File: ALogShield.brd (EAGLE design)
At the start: 53.3 x 78.5 mm, 32 parts, among them U1 DS3231MZ/V+T

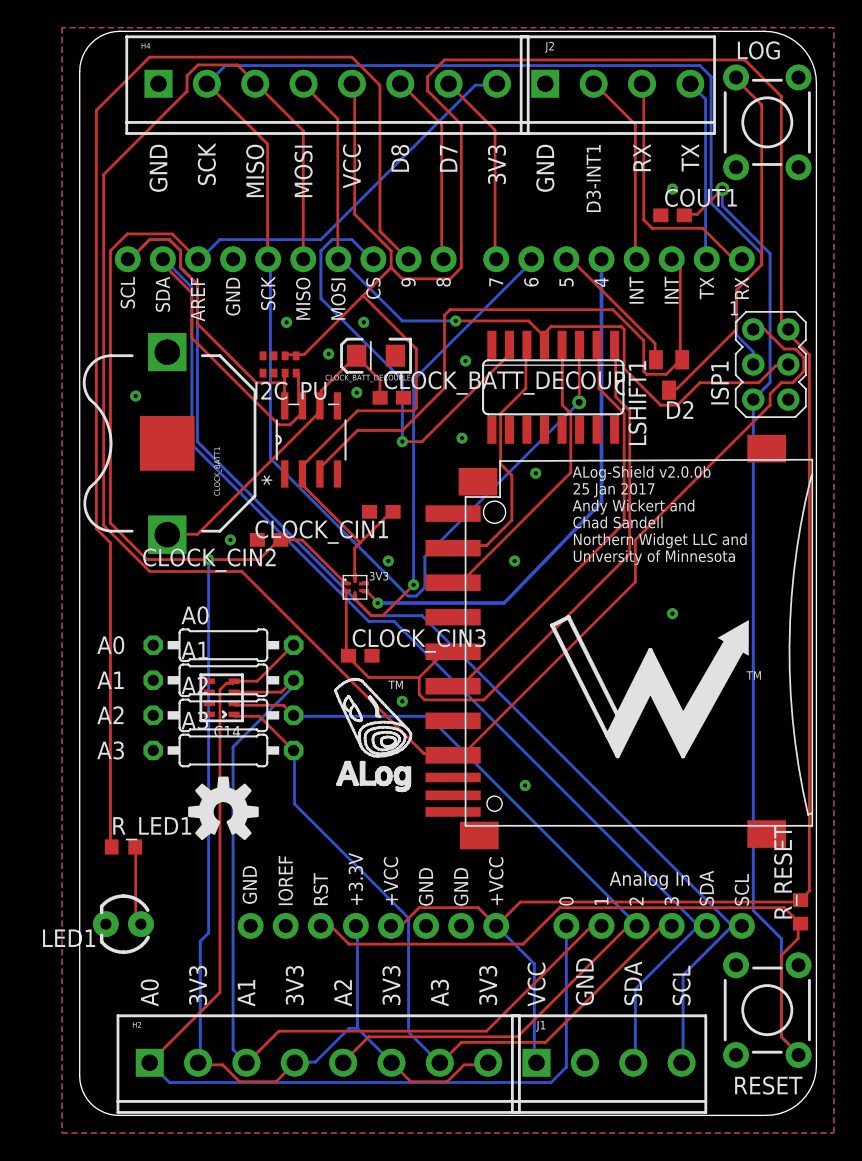
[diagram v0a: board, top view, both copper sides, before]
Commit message: 3V3 with wide pads
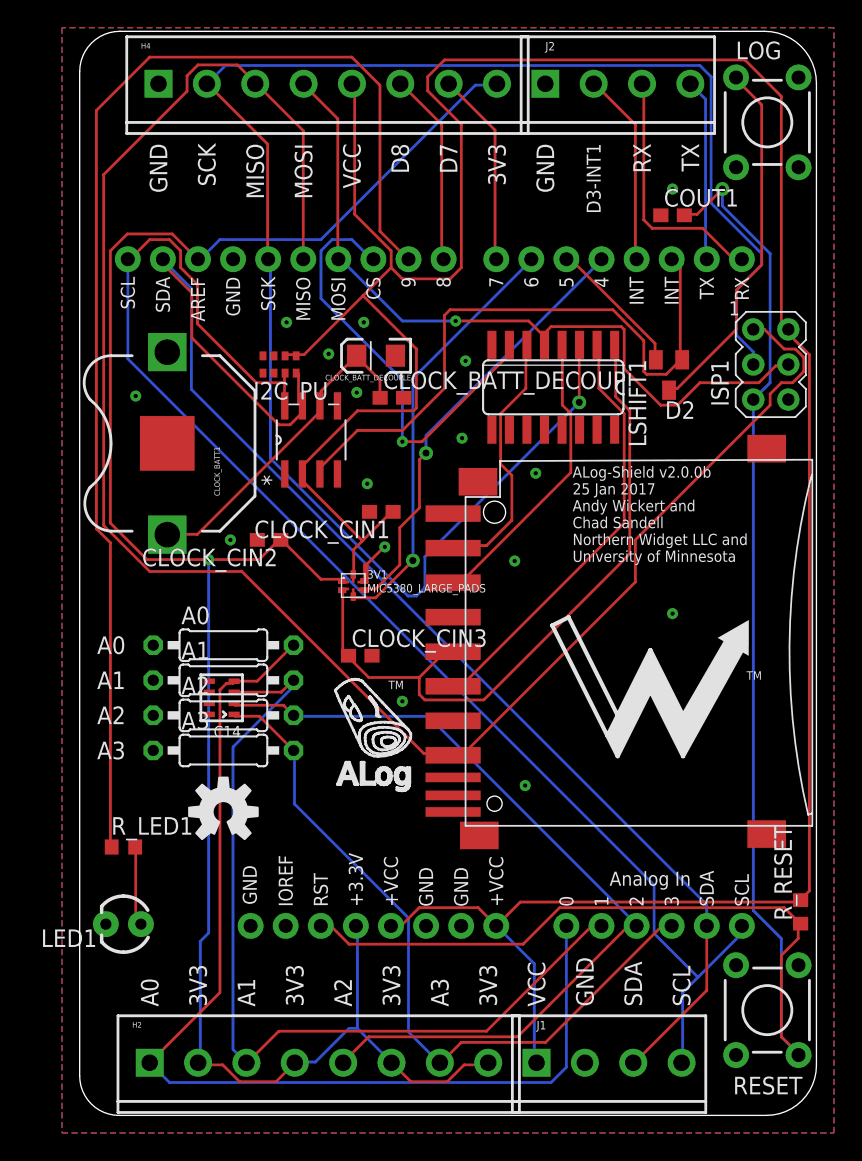
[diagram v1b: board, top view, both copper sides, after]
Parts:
- removed 3V3: (no value), csandell:6-TMLF
- added 3V1: MIC5380_LARGE_PADS, csandell:6-TMLF_SMD_PADS
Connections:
- net +3V3: now also 3V1.1, 3V1.7; no longer 3V3.1
- net D4-SENSE_LDO_SWITCH: now also 3V1.10, 3V1.4; no longer 3V3.4
- net D6-CLOCK_SD_SWITCH: now also 3V1.3, 3V1.9; no longer 3V3.3
- net GND: now also 3V1.11, 3V1.5; no longer 3V3.5
- net VCC: now also 3V1.12, 3V1.6; no longer 3V3.6
- net VDD: now also 3V1.2, 3V1.8; no longer 3V3.2
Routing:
- net D4-SENSE_LDO_SWITCH: track 38.3 -> 31.7 mm
- net SCL: track 106.2 -> 101.8 mm
- net GND: track 0.36 -> 3.59 mm, vias 15 -> 16
- net D6-CLOCK_SD_SWITCH: track 33.1 -> 31.0 mm
- net SDA: track 99.4 -> 97.5 mm

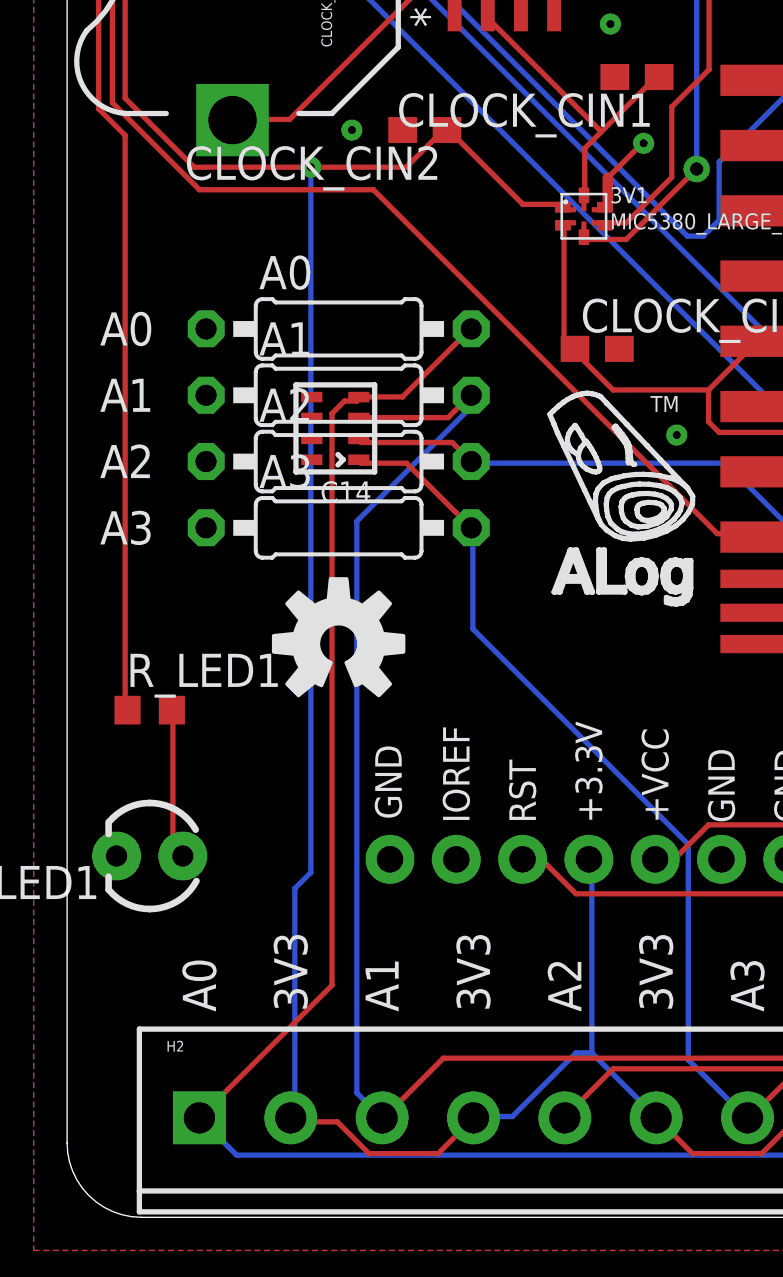
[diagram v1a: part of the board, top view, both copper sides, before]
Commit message: Long pads on cap array: easier soldering, we hope
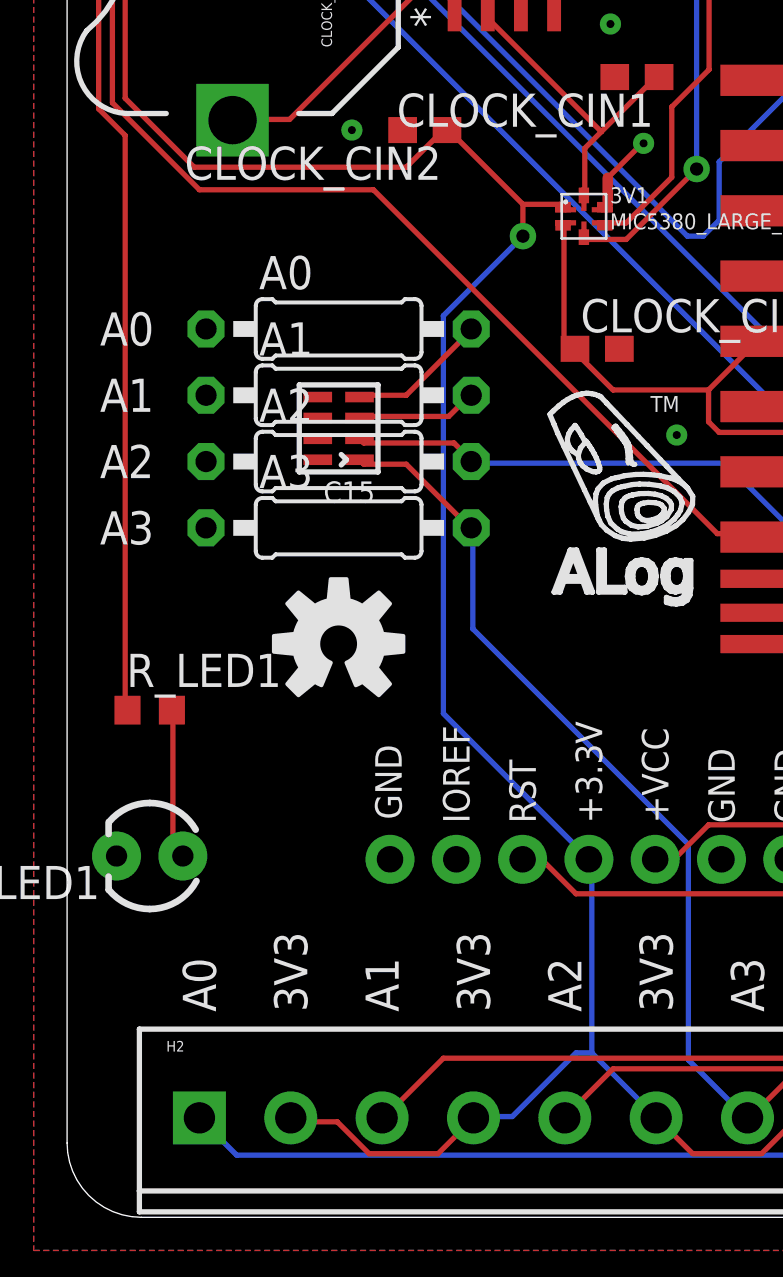
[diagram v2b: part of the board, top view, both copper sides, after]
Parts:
- removed C14: 10nF, rc-master-smd:CECJ-1206
- added C15: 10nF, rc-master-smd:CECJ-CTS-031817
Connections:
- new net N$1: A0.2, C15.D1
- new net N$2: A1.2, C15.C1
- new net N$3: A2.2, C15.B1
- new net N$4: A3.2, C15.A1
- net A0: no longer A0.2, C14.D1
- net A1: no longer A1.2, C14.C1
- net A2: no longer A2.2, C14.B1
- net A3: no longer A3.2, C14.A1
- net GND: now also C15.A2, C15.B2, C15.C2, C15.D2; no longer C14.A2, C14.B2, C14.C2, C14.D2
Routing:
- net A0: track 77.2 -> 41.4 mm
- net A1: track 64.4 -> 29.8 mm
- net +3V3: track 143.6 -> 135.5 mm
- net A3: track 53.3 -> 47.8 mm
- net N$1: track 0.00 -> 5.37 mm
- net N$4: track 0.00 -> 5.36 mm
- net A2: track 61.2 -> 56.5 mm
- net N$3: track 0.00 -> 4.66 mm
- net N$2: track 0.00 -> 4.63 mm
